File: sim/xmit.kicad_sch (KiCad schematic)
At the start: 38 parts

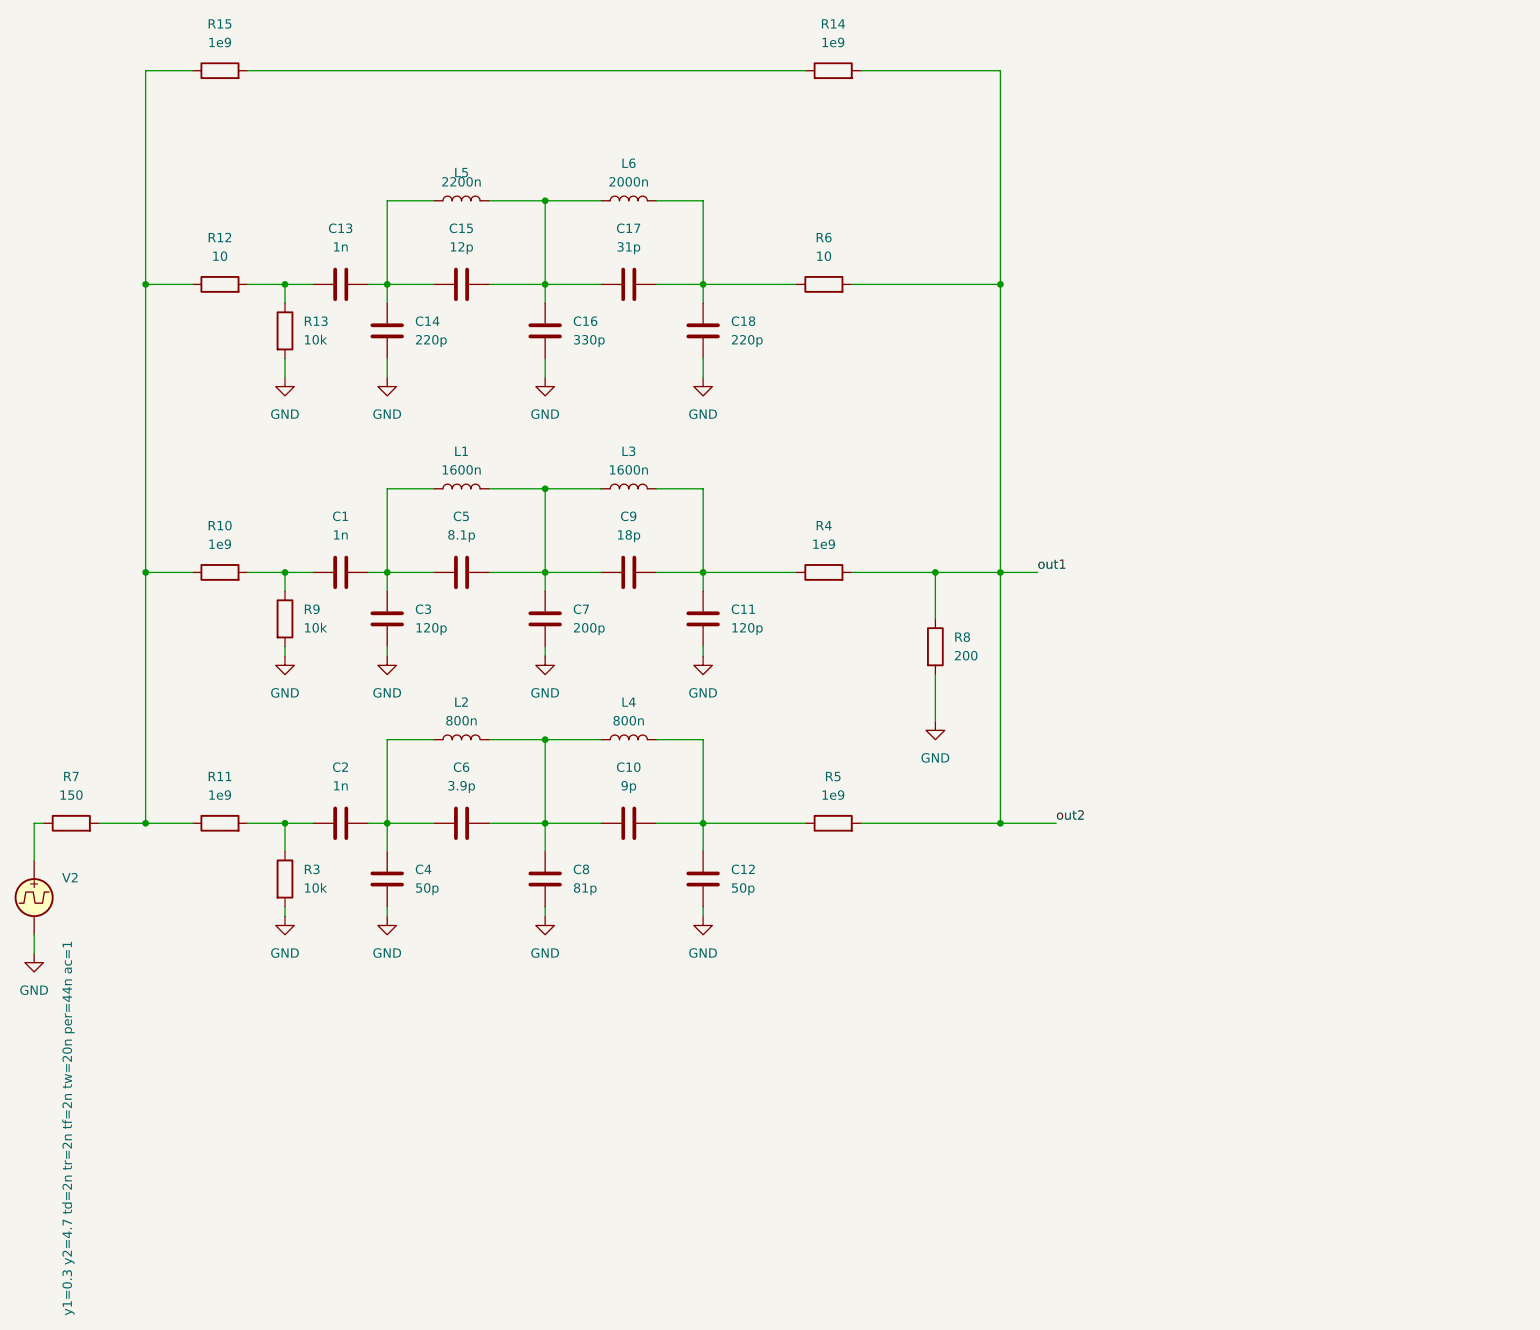
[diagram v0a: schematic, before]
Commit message: More realistic simulations
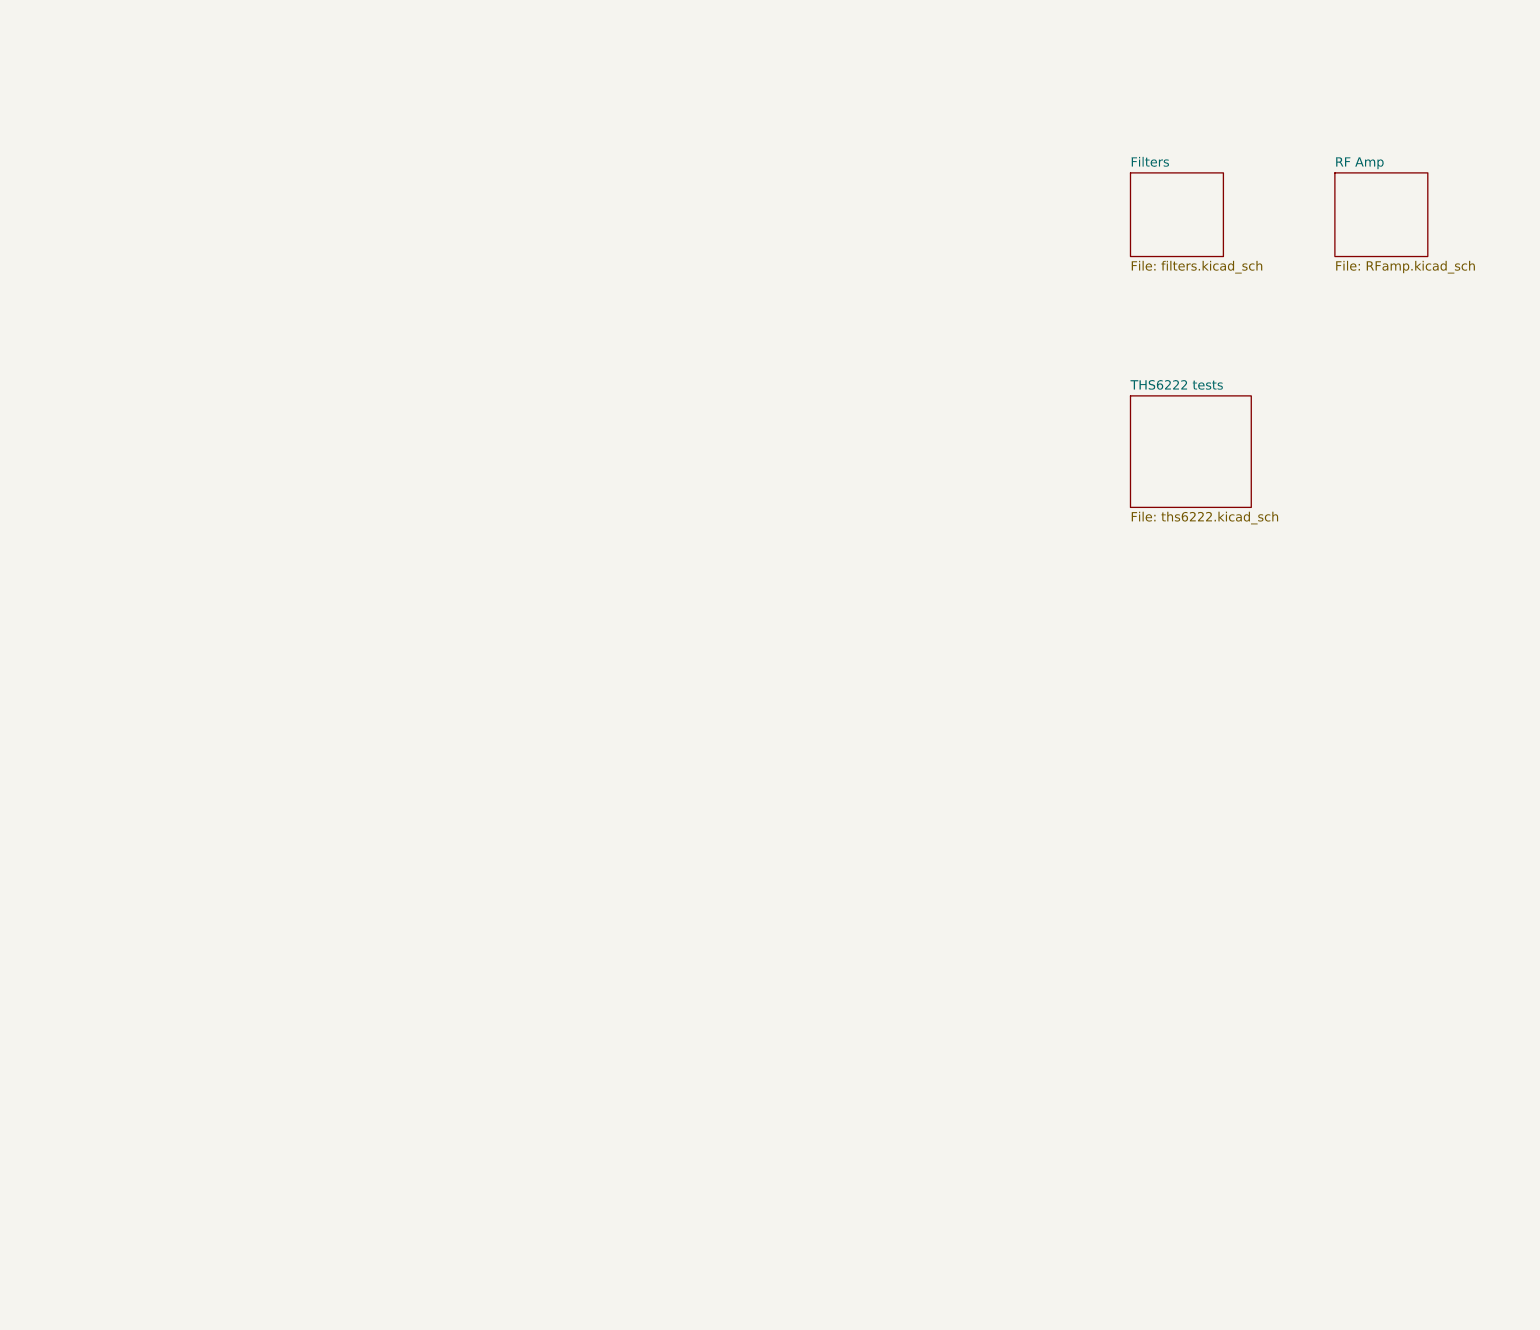
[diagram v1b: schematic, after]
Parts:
- removed C1, C13, C2: 1n, symbol Device:C
- removed C10: 9p, symbol Device:C
- removed C11, C3: 120p, symbol Device:C
- removed C12, C4: 50p, symbol Device:C
- removed C14, C18: 220p, symbol Device:C
- removed C15: 12p, symbol Device:C
- removed C16: 330p, symbol Device:C
- removed C17: 31p, symbol Device:C
- removed C5: 8.1p, symbol Device:C
- removed C6: 3.9p, symbol Device:C
- removed C7: 200p, symbol Device:C
- removed C8: 81p, symbol Device:C
- removed C9: 18p, symbol Device:C
- removed L1, L3: 1600n, symbol Device:L
- removed L2, L4: 800n, symbol Device:L
- removed L5: 2200n, symbol Device:L
- removed L6: 2000n, symbol Device:L
- removed R10, R11, R14, R15, R4, R5: 1e9, symbol Device:R
- removed R12, R6: 10, symbol Device:R
- removed R13, R3, R9: 10k, symbol Device:R
- removed R7: 150, symbol Device:R
- removed R8: 200, symbol Device:R
- removed V2: VPULSE, symbol Simulation_SPICE:VPULSE
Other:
- added sheet Filters (filters.kicad_sch)
- added sheet RF Amp (RFamp.kicad_sch)
- added sheet THS6222 tests (ths6222.kicad_sch)
